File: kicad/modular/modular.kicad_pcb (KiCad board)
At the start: 2 copper layers, 40 parts, among them J1 CONN_PWR, J2 HEADER, J3 HEADER, U1 LM317, U2 LM337, U3 OPA4197, U4 REF5010

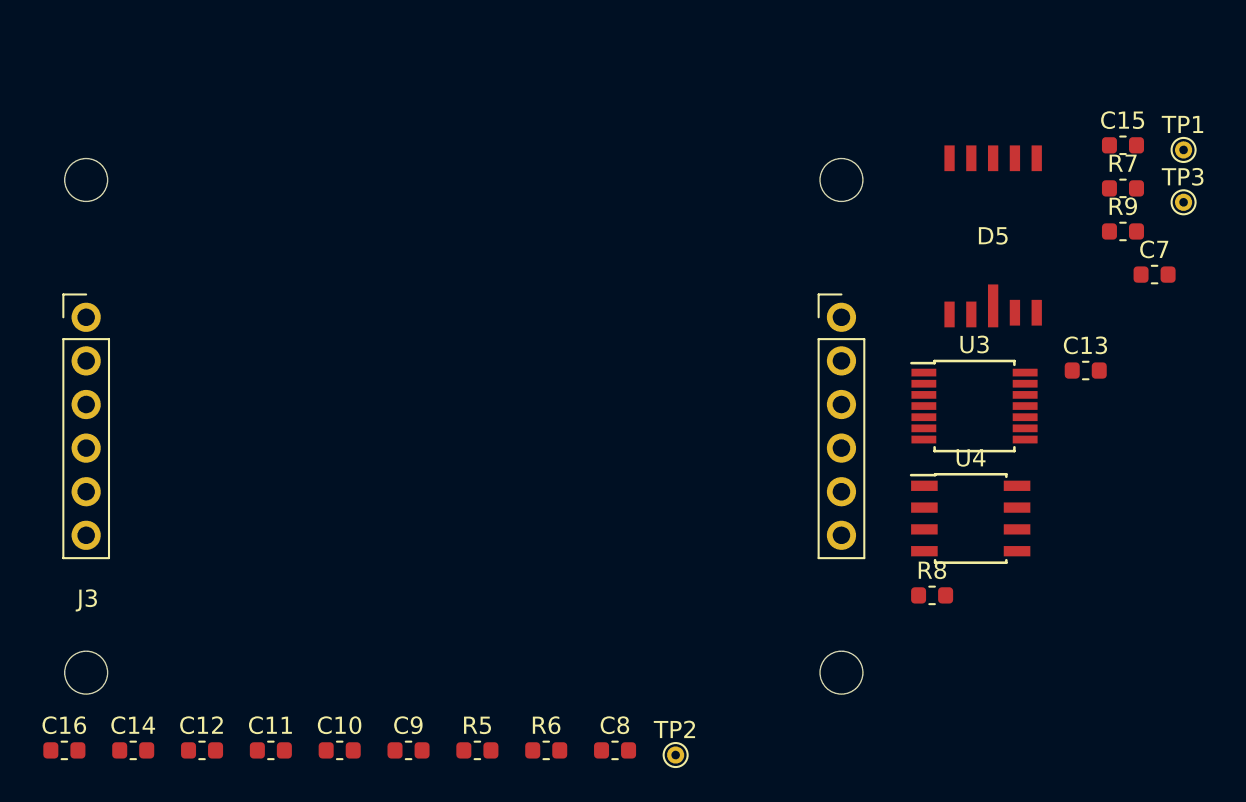
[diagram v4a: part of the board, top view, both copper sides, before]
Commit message: redesigned pcb with more symmetry
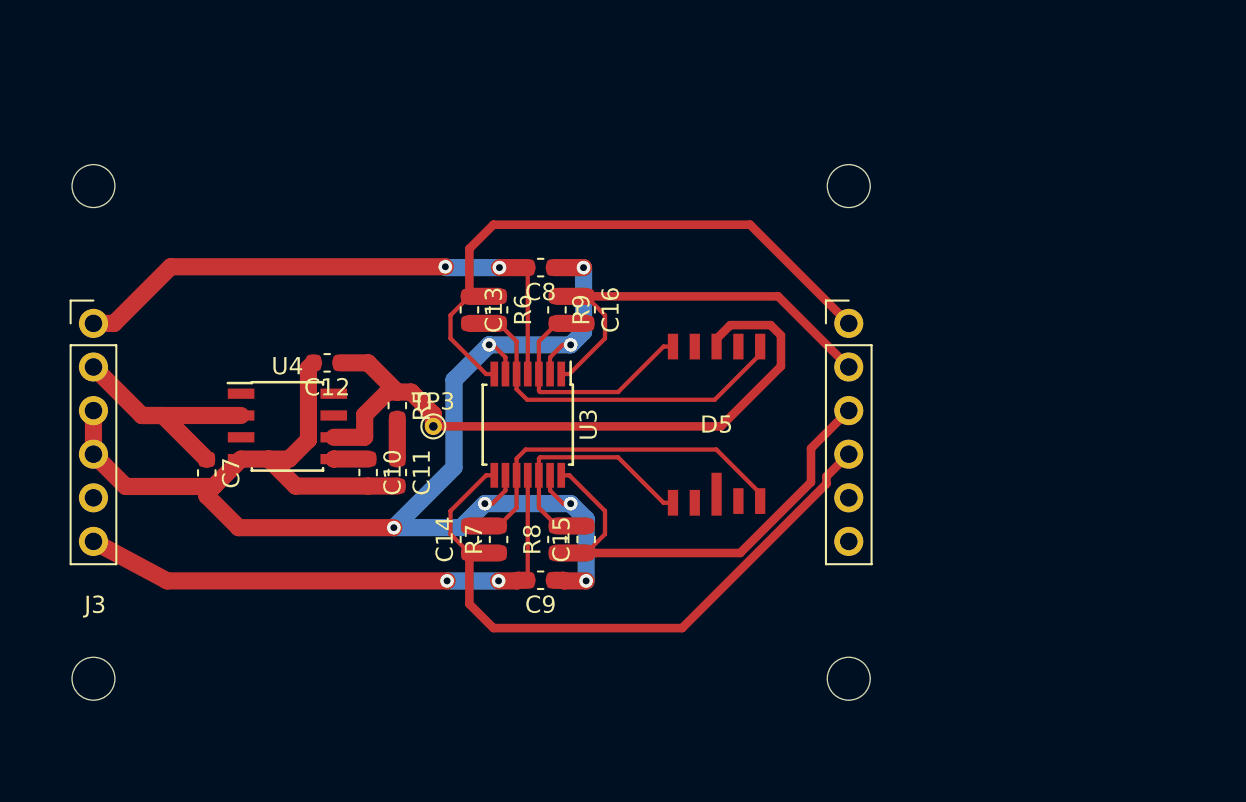
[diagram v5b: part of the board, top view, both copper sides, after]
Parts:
- removed TP1: +12V, TestPoint:TestPoint_THTPad_D1.0mm_Drill0.5mm
- removed TP2: -12V, TestPoint:TestPoint_THTPad_D1.0mm_Drill0.5mm
- moved C7 56.4 mm to (104.8, 135.2), turned to 270 degrees
- moved TP3 45.6 mm to (118.0, 132.5)
- moved R7 41.7 mm to (121.8, 139.1), turned to 90 degrees
- moved U4 40.2 mm to (109.5, 132.5)
- moved C16 39.8 mm to (126.9, 125.7), turned to 270 degrees
- moved C15 38.8 mm to (126.9, 139.1), turned to 90 degrees
- moved C13 36.1 mm to (120.1, 125.7), turned to 270 degrees
- moved R9 33.3 mm to (125.2, 125.7), turned to 270 degrees
- moved C8 28.5 mm to (124.2, 123.2), turned to 180 degrees
- moved U3 26.0 mm to (123.5, 132.4), turned to 270 degrees
- moved R6 25.8 mm to (121.8, 125.7), turned to 270 degrees
- moved C12 23.7 mm to (111.8, 128.8), turned to 180 degrees
- moved C14 23.1 mm to (120.1, 139.1), turned to 90 degrees
- moved R8 22.1 mm to (125.2, 139.1), turned to 90 degrees
- moved R5 20.6 mm to (115.9, 131.3), turned to 270 degrees
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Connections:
- C13 pad 1: /Detector/X1 -> /Detector/X2
- C15 pad 1: /Detector/X2 -> /Detector/X1
- D5 pad 1: Net-(C13-Pad2) -> Net-(C15-Pad2)
- D5 pad 6: Net-(C15-Pad2) -> Net-(C13-Pad2)
- R6 pad 1: /Detector/X1 -> /Detector/X2
- R8 pad 1: /Detector/X2 -> /Detector/X1
- U3 pad 14: /Detector/X2 -> /Detector/X1
- U3 pad 7: /Detector/X1 -> /Detector/X2
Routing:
- net GND: track 85.4 -> 178.6 mm, vias 3 -> 10
- net Net-(C12-Pad1): track 0.00 -> 41.2 mm
- net /Detector/Y1: track 0.00 -> 38.1 mm
- net /Detector/X2: track 0.00 -> 35.9 mm
- net +12V: track 65.4 -> 98.2 mm, vias 0 -> 2
- net -12V: track 58.0 -> 90.0 mm, vias 0 -> 2
- net /Detector/X1: track 0.00 -> 27.9 mm
- net /Detector/Y2: track 0.00 -> 25.0 mm
- net Net-(C14-Pad2): track 0.00 -> 22.0 mm
- net Net-(C13-Pad2): track 0.00 -> 22.0 mm
- net Net-(C16-Pad2): track 0.00 -> 15.0 mm
- net Net-(C15-Pad2): track 0.00 -> 15.0 mm
- net +15V: track 31.2 -> 45.8 mm
- net Net-(C11-Pad1): track 0.00 -> 2.33 mm
- net Net-(C10-Pad1): track 0.00 -> 2.00 mm

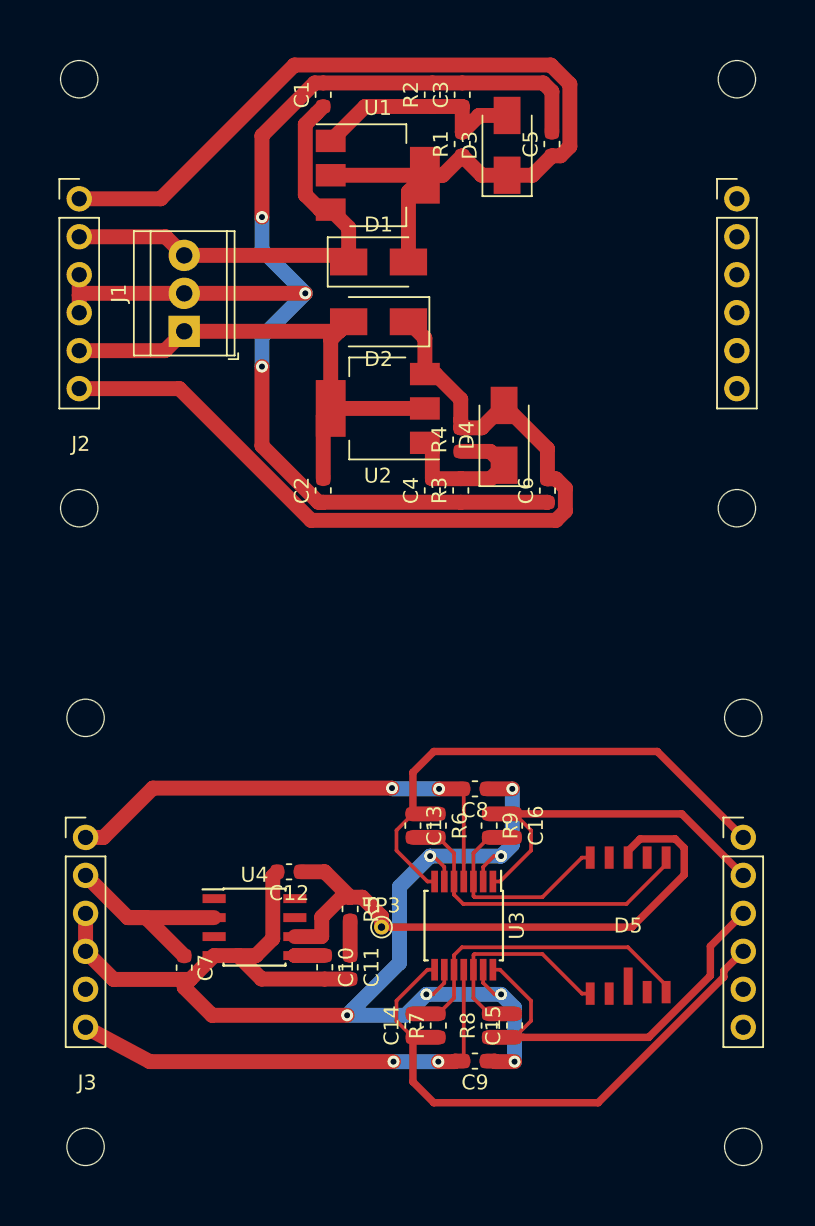
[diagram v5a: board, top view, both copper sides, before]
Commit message: applied pcb design suggestions to modular boards
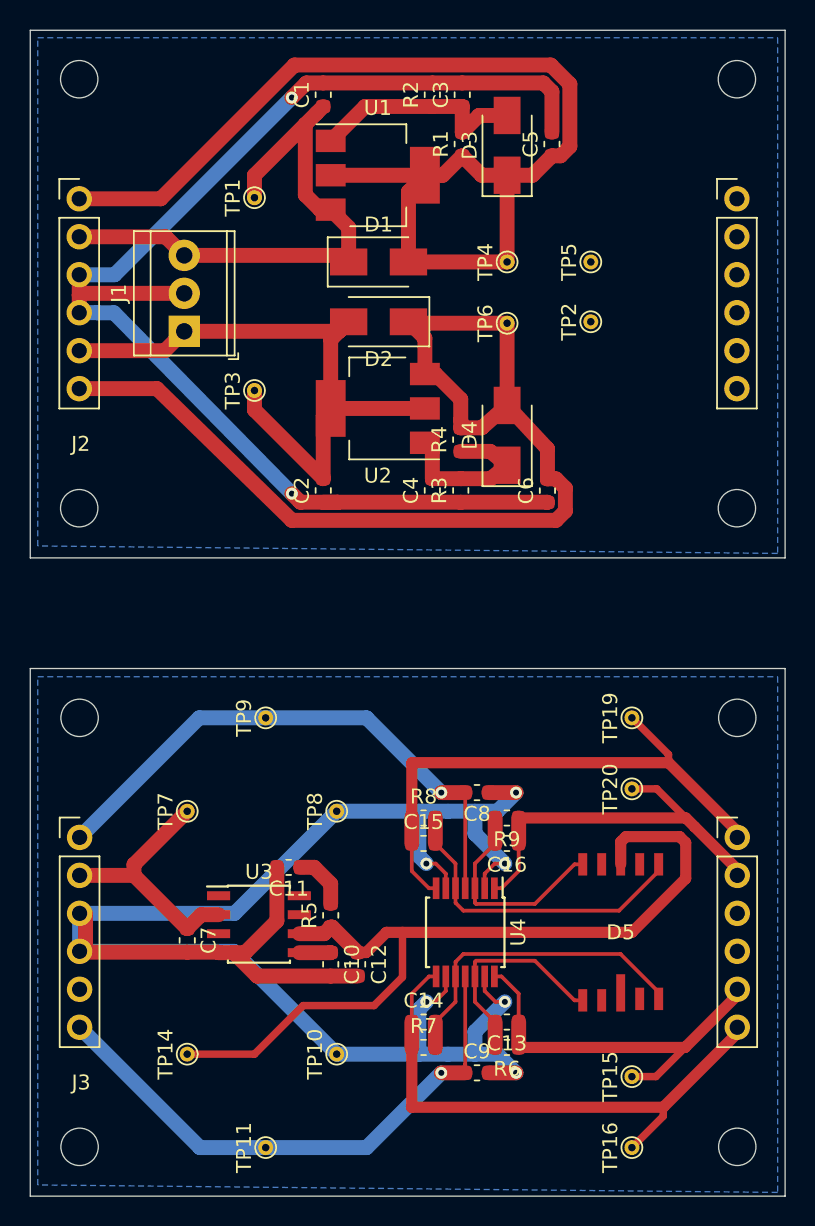
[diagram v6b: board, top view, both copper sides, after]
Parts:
- added TP1: +15V, TestPoint:TestPoint_THTPad_D1.0mm_Drill0.5mm, F.Cu at (109.5, 83.7)
- added TP10: GND, TestPoint:TestPoint_THTPad_D1.0mm_Drill0.5mm, F.Cu at (115.0, 141.0)
- added TP11: -12V, TestPoint:TestPoint_THTPad_D1.0mm_Drill0.5mm, F.Cu at (110.2, 147.2)
- added TP14: BIAS, TestPoint:TestPoint_THTPad_D1.0mm_Drill0.5mm, F.Cu at (105.0, 141.0)
- added TP15: U1, TestPoint:TestPoint_THTPad_D1.0mm_Drill0.5mm, F.Cu at (134.8, 142.5)
- added TP16: U3, TestPoint:TestPoint_THTPad_D1.0mm_Drill0.5mm, F.Cu at (134.8, 147.2)
- added TP19: U2, TestPoint:TestPoint_THTPad_D1.0mm_Drill0.5mm, F.Cu at (134.8, 118.5)
- added TP2: GND, TestPoint:TestPoint_THTPad_D1.0mm_Drill0.5mm, F.Cu at (132.0, 92.0)
- added TP20: U4, TestPoint:TestPoint_THTPad_D1.0mm_Drill0.5mm, F.Cu at (134.8, 123.2)
- added TP4: +12V, TestPoint:TestPoint_THTPad_D1.0mm_Drill0.5mm, F.Cu at (126.4, 88.0)
- added TP5: GND, TestPoint:TestPoint_THTPad_D1.0mm_Drill0.5mm, F.Cu at (132.0, 88.0)
- added TP6: -12V, TestPoint:TestPoint_THTPad_D1.0mm_Drill0.5mm, F.Cu at (126.4, 92.1)
- added TP7: +15V, TestPoint:TestPoint_THTPad_D1.0mm_Drill0.5mm, F.Cu at (105.0, 124.8)
- added TP8: GND, TestPoint:TestPoint_THTPad_D1.0mm_Drill0.5mm, F.Cu at (115.0, 124.8)
- added TP9: +12V, TestPoint:TestPoint_THTPad_D1.0mm_Drill0.5mm, F.Cu at (110.2, 118.5)
- TP3: value BIAS -> -15V
- U3: value OPA4197 -> REF5010; footprint Package_SO:TSSOP-14_4.4x5mm_P0.65mm -> Package_SO:SOIC-8_3.9x4.9mm_P1.27mm
- U4: value REF5010 -> OPA4197; footprint Package_SO:SOIC-8_3.9x4.9mm_P1.27mm -> Package_SO:TSSOP-14_4.4x5mm_P0.65mm
- moved TP3 36.9 mm to (109.5, 96.6), turned to 90 degrees
- moved R6 15.5 mm to (126.4, 140.6), turned to 180 degrees
- moved C13 14.6 mm to (126.4, 138.8), turned to 180 degrees
- moved R8 14.6 mm to (120.8, 125.2), turned to 0 degrees
- moved U4 14.1 mm to (123.6, 132.8), turned to 270 degrees
- moved U3 13.7 mm to (109.8, 132.3), turned to 0 degrees
- moved C15 13.6 mm to (120.8, 126.9), turned to 0 degrees
- moved C11 7.85 mm to (111.8, 128.5), turned to 180 degrees
- moved C12 7.70 mm to (116.4, 135.0), turned to 270 degrees
- moved C7 1.84 mm to (105.0, 133.4)
- moved R7 1.76 mm to (120.8, 140.6), turned to 0 degrees
- moved R5 1.37 mm to (114.6, 131.7), turned to 90 degrees
- moved C16 1.29 mm to (126.4, 126.9), turned to 180 degrees
- moved R9 1.29 mm to (126.4, 125.2), turned to 180 degrees
- moved C9 0.80 mm to (124.4, 142.2), turned to 0 degrees
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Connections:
- C13 pad 1: /Detector/X2 -> /Detector/X1
- C15 pad 1: /Detector/X1 -> /Detector/X2
- C9 pad 1: GND -> -12V
- C9 pad 2: -12V -> GND
- D5 pad 1: Net-(C15-Pad2) -> Net-(C13-Pad2)
- D5 pad 6: Net-(C13-Pad2) -> Net-(C15-Pad2)
- R6 pad 1: /Detector/X2 -> /Detector/X1
- R8 pad 1: /Detector/X1 -> /Detector/X2
- TP3 pad 1: Net-(C12-Pad1) -> -15V
- U3 pad 1: /Detector/Y2 -> Net-(U3-Pad1)
- U3 pad 2: GND -> +15V
- U3 pad 3: Net-(C16-Pad2) -> Net-(U3-Pad3)
- U3 pad 4: +12V -> GND
- U3 pad 5: Net-(C13-Pad2) -> Net-(C10-Pad1)
- U3 pad 6: GND -> Net-(C12-Pad1)
- U3 pad 7: /Detector/X2 -> Net-(U3-Pad7)
- U3 pad 8: /Detector/Y1 -> Net-(U3-Pad8)
- U4 pad 1: Net-(U4-Pad1) -> /Detector/Y2
- U4 pad 2: +15V -> GND
- U4 pad 3: Net-(U4-Pad3) -> Net-(C16-Pad2)
- U4 pad 4: GND -> +12V
- U4 pad 5: Net-(C10-Pad1) -> Net-(C15-Pad2)
- U4 pad 6: Net-(C12-Pad1) -> GND
- U4 pad 7: Net-(U4-Pad7) -> /Detector/X2
- U4 pad 8: Net-(U4-Pad8) -> /Detector/Y1
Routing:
- net GND: track 178.6 -> 213.7 mm, vias 10 -> 8
- net -12V: track 90.0 -> 107.8 mm, vias 2 -> 1
- net +12V: track 98.2 -> 115.3 mm, vias 2 -> 1
- net Net-(C12-Pad1): track 41.2 -> 56.9 mm
- net +15V: track 45.8 -> 54.1 mm
- net -15V: track 36.3 -> 44.1 mm
- net Net-(C13-Pad2): track 22.0 -> 14.6 mm
- net Net-(C15-Pad2): track 15.0 -> 21.6 mm
- net /Detector/Y2: track 25.0 -> 27.5 mm
- net /Detector/X2: track 35.9 -> 37.6 mm
- net Net-(C11-Pad1): track 2.33 -> 3.81 mm
- net /Detector/X1: track 27.9 -> 26.7 mm
- added copper zone on B.Cu, net GND
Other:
- board outline added: 50.5 x 78 mm
